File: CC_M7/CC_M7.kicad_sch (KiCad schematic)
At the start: 0 parts

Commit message: Connectors updated
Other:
- note added: "15V to 5V"
- note removed: "12V to 5V"
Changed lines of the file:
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@@
 		(comment 1 "Stm32 F7 Control Cart")
 	)
-	(text "12V to 5V"
+	(text "15V to 5V"
 		(exclude_from_sim no)
-		(at 116.332 85.344 0)
+		(at 34.798 69.596 0)
 		(effects
 			(font
 				(size 1.27 1.27)
+				(thickness 0.254)
+				(bold yes)
 			)
 		)
@@
 	(text "USB Port\nPWM Outputs\nUART,I2C,CAN Pins\nGPS Pins\n2X20 RASBERRY PI 0 COMPATIBLE PINS"
 		(exclude_from_sim no)
-		(at 109.474 128.524 0)
+		(at 29.972 120.904 0)
 		(effects
 			(font
 				(size 1.27 1.27)
+				(thickness 0.254)
+				(bold yes)
 			)
 			(justify left)
@@
 	(text "Telemetry"
 		(exclude_from_sim no)
-		(at 116.84 232.156 0)
+		(at 34.29 217.678 0)
 		(effects
 			(font
 				(size 1.27 1.27)
+				(thickness 0.254)
+				(bold yes)
 			)
 		)
@@
 	(text "STM32H743VIT6 Pins Connections\nVoltage Read\nFilters\nStm32h743 Requirments"
 		(exclude_from_sim no)
-		(at 109.22 38.354 0)
+		(at 29.972 25.4 0)
 		(effects
 			(font
 				(size 1.27 1.27)
+				(thickness 0.254)
+				(bold yes)
 			)
 			(justify left)
@@
 	(text "IMU:BNI088\nPressure Sensor:BMP388\nCompass:BMM150\n"
 		(exclude_from_sim no)
-		(at 110.236 176.53 0)
+		(at 30.48 167.386 0)
 		(effects
 			(font
 				(size 1.27 1.27)
+				(thickness 0.254)
+				(bold yes)
 			)
 			(justify left)

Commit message: nrf
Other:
- note added: "5V to 3.3V"
- note added: "IMU:BMI088 Pressure Sensor:BMP388 Compass:BMM150 EEPROM:24AAOIT"
- note removed: "IMU:BNI088 Pressure Sensor:BMP388 Compass:BMM150"
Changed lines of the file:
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@@
 	(text "15V to 5V"
 		(exclude_from_sim no)
-		(at 34.798 69.596 0)
+		(at 34.544 69.596 0)
+		(effects
+			(font
+				(size 1.27 1.27)
+				(thickness 0.254)
+				(bold yes)
+			)
+		)
+	)
+	(text "5V to 3.3V"
+		(exclude_from_sim no)
+		(at 34.798 72.644 0)
 		(effects
 			(font
@@
 		)
 	)
-	(text "IMU:BNI088\nPressure Sensor:BMP388\nCompass:BMM150\n"
+	(text "IMU:BMI088\nPressure Sensor:BMP388\nCompass:BMM150\nEEPROM:24AAOIT\n"
 		(exclude_from_sim no)
-		(at 30.48 167.386 0)
+		(at 30.48 168.656 0)
 		(effects
 			(font

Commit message: Changes updated @ CCM7.docx
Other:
- note added: "USB Port PWM Outputs UART,I2C GPS Pins 2X20 RASBERRY PI 0 COMPATIBLE PINS"
- note removed: "USB Port PWM Outputs UART,I2C,CAN Pins GPS Pins 2X20 RASBERRY PI 0 COMPATIBLE PINS"
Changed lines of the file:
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@@
 		)
 	)
-	(text "USB Port\nPWM Outputs\nUART,I2C,CAN Pins\nGPS Pins\n2X20 RASBERRY PI 0 COMPATIBLE PINS"
+	(text "USB Port\nPWM Outputs\nUART,I2C\nGPS Pins\n2X20 RASBERRY PI 0 COMPATIBLE PINS"
 		(exclude_from_sim no)
 		(at 29.972 120.904 0)

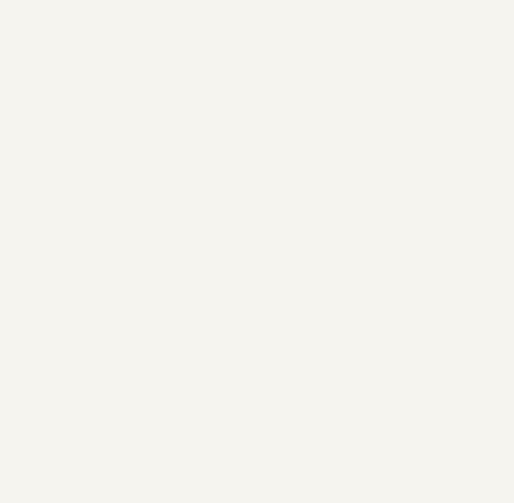
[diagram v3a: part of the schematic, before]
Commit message: Mounting Hole added.
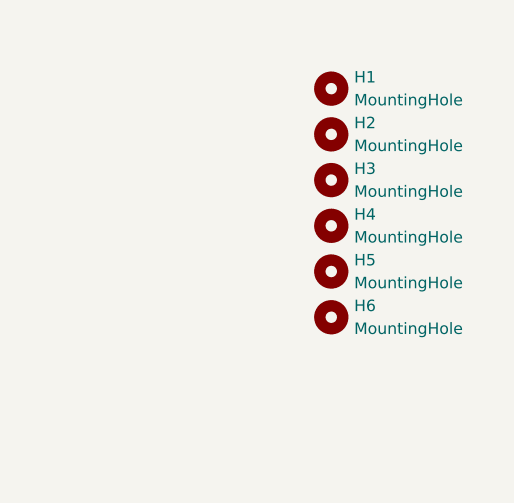
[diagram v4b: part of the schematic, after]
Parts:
- added H1, H2, H3, H4, H5, H6: MountingHole, MountingHole:MountingHole_3.2mm_M3_ISO14580_Pad, symbol Mechanical:MountingHole

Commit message: warning check
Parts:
- H1, H2, H3, H4, H5, H6: footprint MountingHole:MountingHole_3.2mm_M3_ISO14580_Pad -> MountingHole:CCMountingHole
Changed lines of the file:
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@@
 			)
 		)
-		(property "Footprint" "MountingHole:MountingHole_3.2mm_M3_ISO14580_Pad"
+		(property "Footprint" "MountingHole:CCMountingHole"
 			(at 157.48 35.56 0)
 			(effects
@@
 			)
 		)
-		(property "Footprint" "MountingHole:MountingHole_3.2mm_M3_ISO14580_Pad"
+		(property "Footprint" "MountingHole:CCMountingHole"
 			(at 157.48 30.48 0)
 			(effects
@@
 			)
 		)
-		(property "Footprint" "MountingHole:MountingHole_3.2mm_M3_ISO14580_Pad"
+		(property "Footprint" "MountingHole:CCMountingHole"
 			(at 157.48 40.64 0)
 			(effects
@@
 			)
 		)
-		(property "Footprint" "MountingHole:MountingHole_3.2mm_M3_ISO14580_Pad"
+		(property "Footprint" "MountingHole:CCMountingHole"
 			(at 157.48 45.72 0)
 			(effects
@@
 			)
 		)
-		(property "Footprint" "MountingHole:MountingHole_3.2mm_M3_ISO14580_Pad"
+		(property "Footprint" "MountingHole:CCMountingHole"
 			(at 157.48 50.8 0)
 			(effects
@@
 			)
 		)
-		(property "Footprint" "MountingHole:MountingHole_3.2mm_M3_ISO14580_Pad"
+		(property "Footprint" "MountingHole:CCMountingHole"
 			(at 157.48 25.4 0)
 			(effects
